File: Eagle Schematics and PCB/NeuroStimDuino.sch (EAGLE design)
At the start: 161 parts, among them IC1 DSPIC33FJ256GP506A-I_PT, IC10 OPA140AID, IC13 TPS73633DBVR, IC14 MIC3975-5.0YMM-TR, IC2 FT232RL, IC3 HCPL0531, IC4 HCPL0531, IC5 INA149AID, IC6 TSC2011IDT, IC7 OPA140AID, IC8 INA149AID, J1 22-27-2051-05, J2 47346-0001, J5 TMS-103-02-L-S, J6 TMS-103-02-L-S, J7 CON-SOCJ-2155, K1 LBB110P, Q1 MJE350, Q2 MJE340, Q3 MJE350, Q4 MJE340, Q8 MMBT3906, U1 AD826ARZ, U2 LT1991IMSPBF, U3 LT1991IMSPBF, U4 MCP41HV31-103E/ST, U5 MCP41HV31-103E/ST, U6 LTC4412HS6TRMPBF, U7 PMV48XP,215TO-236_SOT23_NEX-L, U8 PDME1-S5-D5-S, U9 MAX6018BEUR16+T

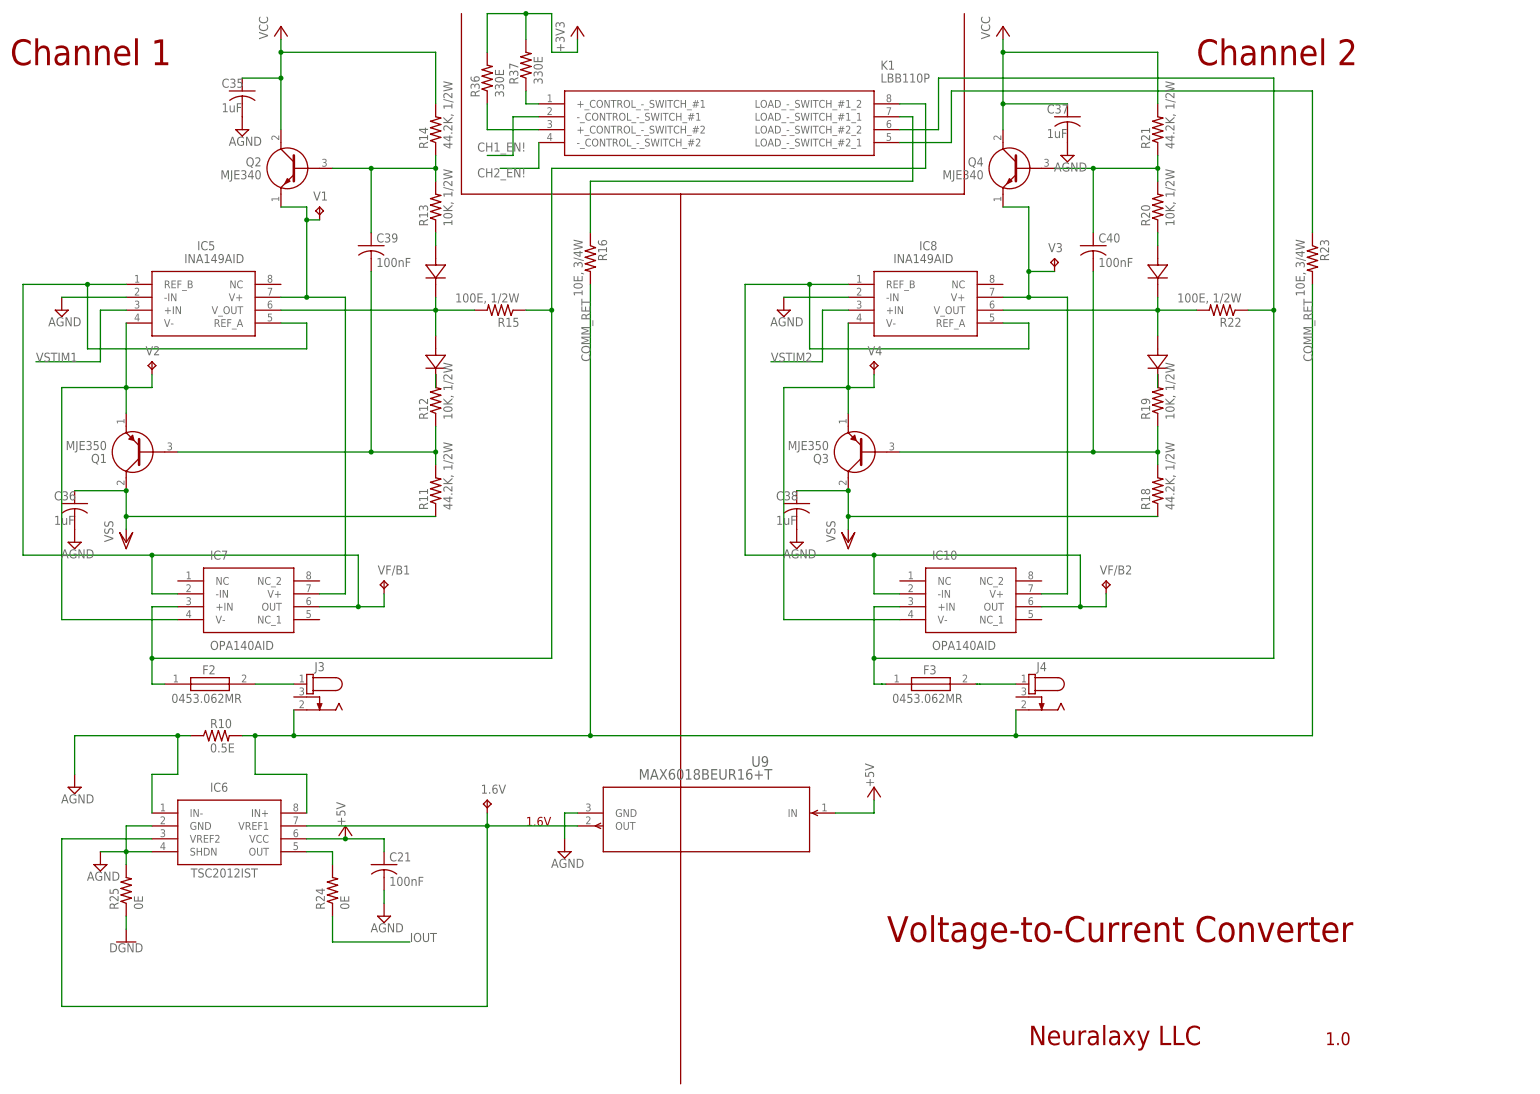
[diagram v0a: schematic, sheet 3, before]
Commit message: NeuroStimDuino_v1.1 schematic and PCB files
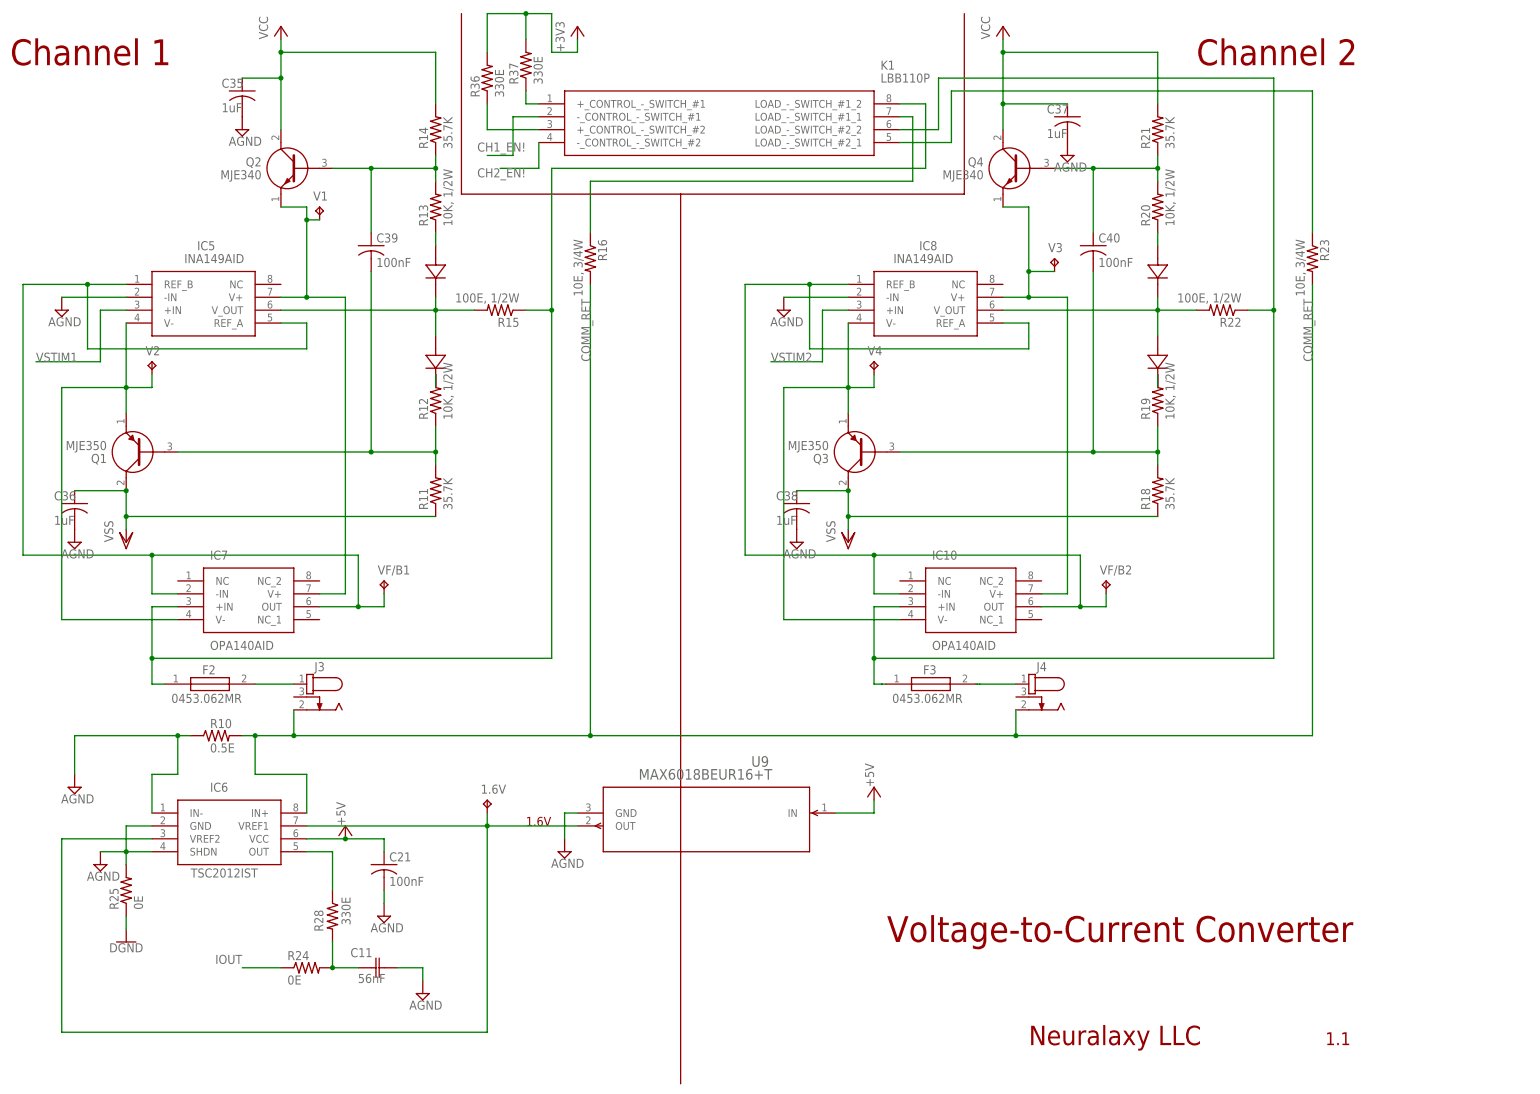
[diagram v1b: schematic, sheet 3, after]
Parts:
- added C11: 56nF, Capacitor_56nF:C0603C563J4RACTU
- added R28: 330E, rcl:R-US_R0603
- IC6: value TSC2011IDT -> TSC2012IST; device SamacSys_Parts:TSC2011IDT -> SamacSys_Parts:TSC2012IST
- R11, R14, R18, R21: value 44.2K, 1/2W -> 35.7K
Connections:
- net PWM10 renamed D10
- net PWM9 renamed D9
- new net N$28: C11.1, R24.2, R28.2
- net AGND: now also C11.2
- net N$19: now also R28.1; no longer R24.2
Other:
- note added: "(3-19-2021) Fixed footprint for MCP41HV31"
- note added: "(5-17-2021) Added anti-aliasing filter at ADC input. RC lowpass filter with R = 330E, C = 56nF to get a cutoff freq of 8.61 kHz and rise time of 40 usec."
- note added: "(5-25-2021) Changed values of resistors R11, R14, R18, R21 from 44.2K to 35.7K to increase compliance voltage"
- note added: "1.1"
- note removed: "1.0"
- moved on the sheet: R24
